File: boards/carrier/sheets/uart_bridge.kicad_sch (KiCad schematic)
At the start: 9 parts

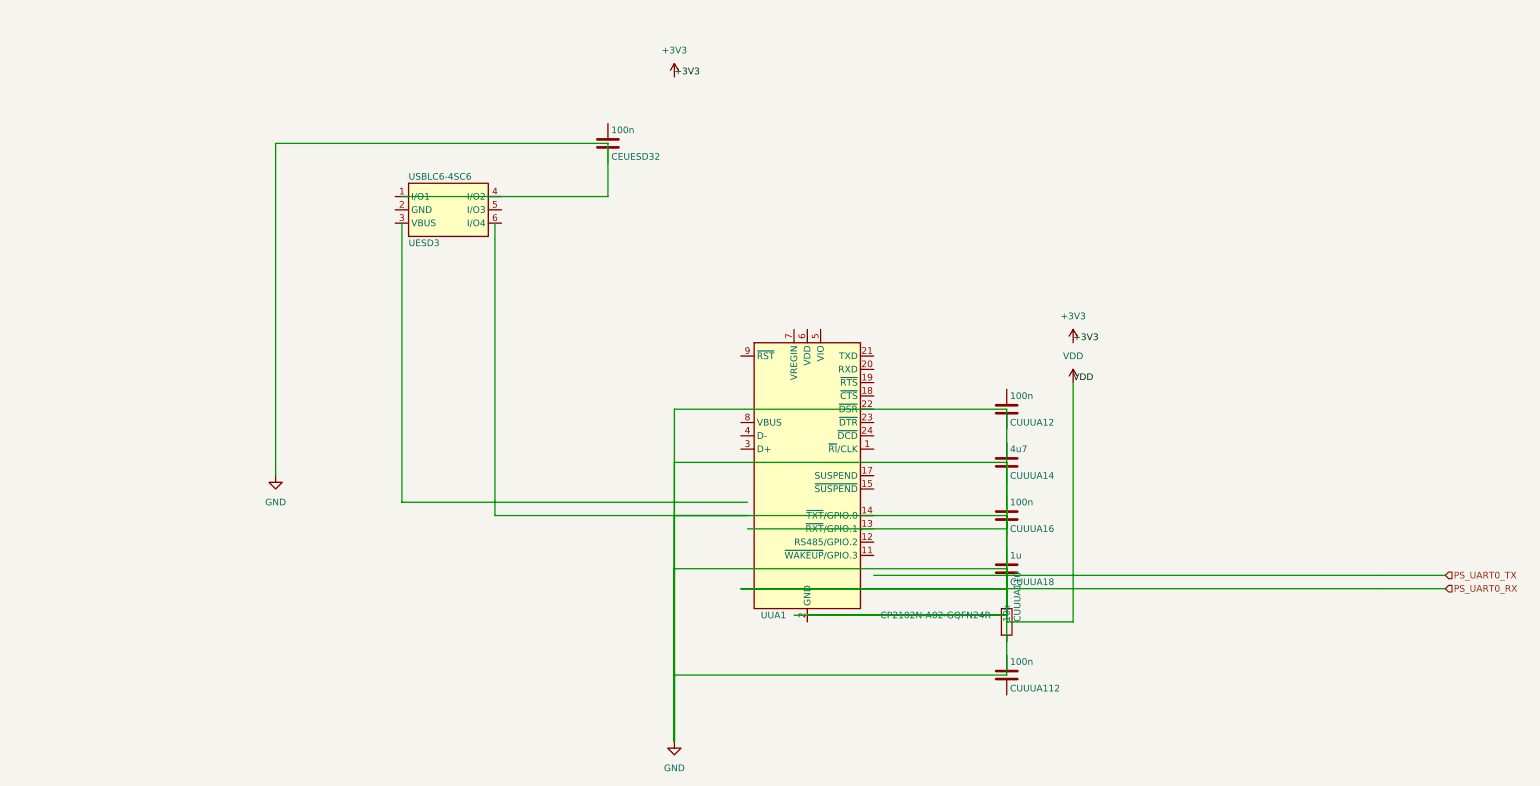
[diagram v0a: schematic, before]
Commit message: Stage 6 (1/4): add power_mon, usbc_otg, uart_bridge blocks
power_mon: INA226AIDGSR high-side current/power monitor on +VIN, VS = +3V3,
I2C2 readback + ALERT_N to the STM32 co-processor. Single IC; R_sense and
differential input filter come from INA226_REFCIRCUIT.external_parts.

usbc_otg: dedicated USB-C OTG port (second USBC_16P receptacle) with a
TPS2051CDBVR current-limited VBUS load switch gating +VIN → VBUS_OTG.
USB 2.0 D+/D- to the SoM PHY; STM32 controls VBUS_EN and reads OC_N.
Connector reuses USBC_DEVICE_REFCIRCUIT (5.1k Rd sink advertisement
+ 1M/100nF shield discharge).

uart_bridge: CP2102N-A02-GQFN24R USB-to-UART bridge for the Zynq PS UART0
debug console. Self-powered via internal LDO (REGIN = +VIN from a dedicated
micro-USB-B receptacle, Connector:USB_B_Micro). UART0 RXD/TXD with
RTS_N/CTS_N hardware flow control to the Zynq PS.

All three blocks build cleanly through the full pipeline:

    $ python -m zynq_eda --board carrier
    built 5 block(s): power, usb_pd, power_mon, usbc_otg, uart_bridge

ERC errors are pre-existing and tracked by the parallel cluster-fix work;
the new block builders themselves are correct (sheets are non-empty,
hierarchical labels land on the requested edges).

Co-Authored-By: Claude Opus 4.7 <noreply@anthropic.com>
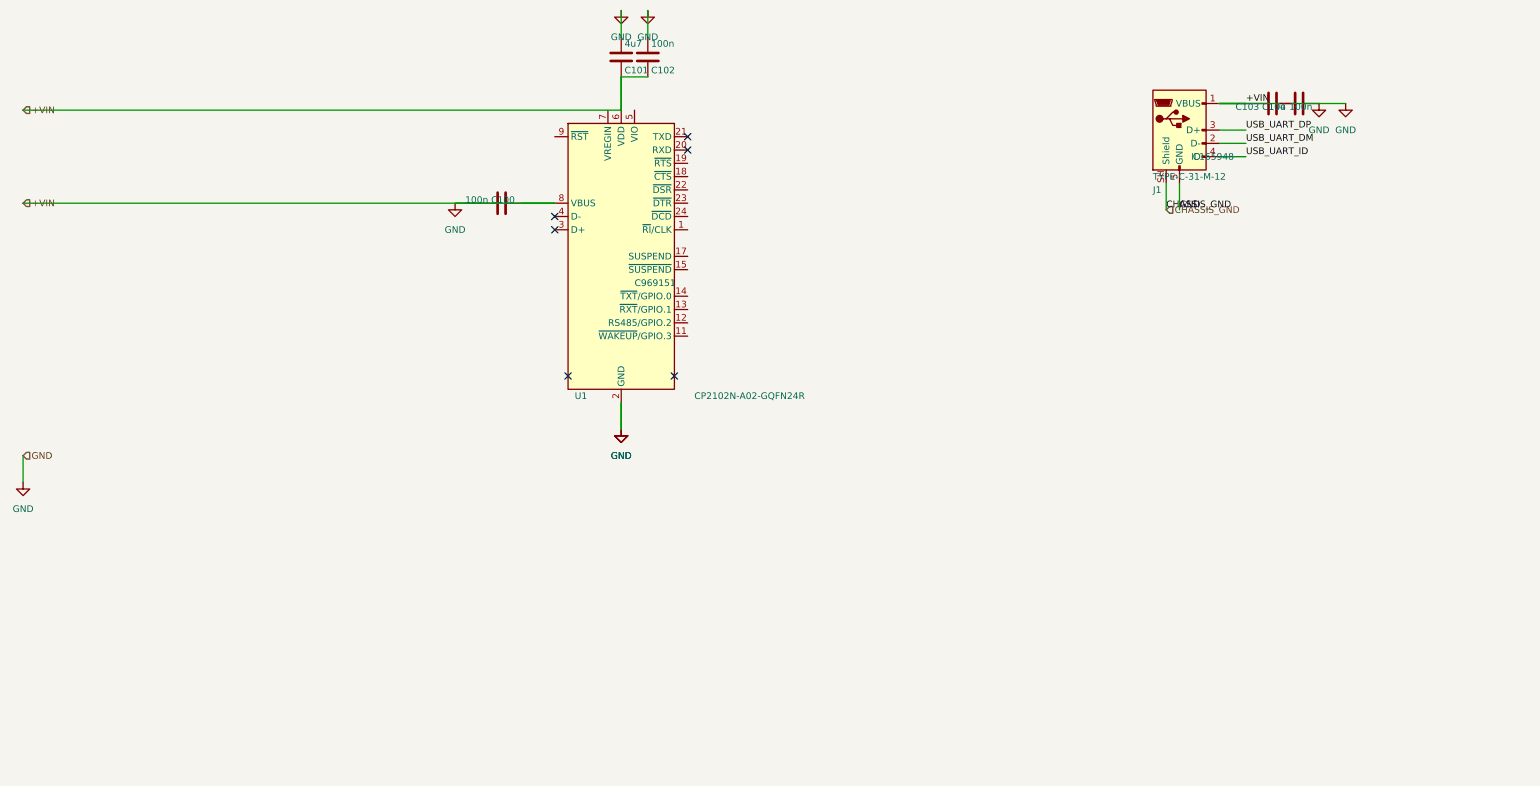
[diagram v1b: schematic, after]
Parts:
- removed CEUESD32, CUUUA112, CUUUA12, CUUUA16: 100n, Capacitor_SMD:C_0402_1005Metric, symbol Device:C
- removed CUUUA110: 10k, Resistor_SMD:R_0402_1005Metric, symbol Device:R
- removed CUUUA14: 4u7, Capacitor_SMD:C_0402_1005Metric, symbol Device:C
- removed CUUUA18: 1u, Capacitor_SMD:C_0402_1005Metric, symbol Device:C
- removed UESD3: USBLC6-4SC6, Package_TO_SOT_SMD:SOT-23-6, symbol carrier:USBLC6-4SC6
- removed UUA1: CP2102N-A02-GQFN24R, Package_DFN_QFN:QFN-24-1EP_4x4mm_P0.5mm_EP2.6x2.6mm, symbol Interface_USB:CP2102N-Axx-xQFN24
- added C100, C102, C104: 100n, Capacitor_SMD:C_0402_1005Metric, symbol Device:C
- added C101: 4u7, Capacitor_SMD:C_0402_1005Metric, symbol Device:C
- added C103: 10u, Capacitor_SMD:C_0402_1005Metric, symbol Device:C
- added J1: TYPE-C-31-M-12, Connector_USB:USB_C_Receptacle_HRO_TYPE-C-31-M-12, symbol Connector:USB_B_Micro
- added U1: CP2102N-A02-GQFN24R, Package_DFN_QFN:QFN-24-1EP_4x4mm_P0.5mm_EP2.6x2.6mm, symbol Interface_USB:CP2102N-Axx-xQFN24
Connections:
- net GND: now also C100.1, C100.2, C101.1, C101.2, C102.1, C102.2, C103.1, C103.2, C104.1, C104.2, J1.1 (VBUS), J1.5 (GND), U1.2 (GND), U1.25 (GND), U1.6 (VDD), U1.8 (VBUS)
- new net CHASSIS_GND: J1.SH (Shield)
- new net USB_UART_DM: J1.2 (D-)
- new net USB_UART_DP: J1.3 (D+)
- new net USB_UART_ID: J1.4 (ID)
- no-connect marks 0 -> 6
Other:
- title: USB-UART Bridge (CP2102N + USBLC6) -> USB-UART Bridge (CP2102N → Zynq PS UART0)
